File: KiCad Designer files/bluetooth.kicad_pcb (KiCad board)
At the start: 32 copper layers, 30.5 x 38.1 mm, 53 parts, among them U1 Multi-protocol Bluetooth Low 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, U1 O, U10 O, U11 O, U12 O, U13 O, U14 O, U15 O, U16 O, U17 O, U18 O, U19 O, U2 O, U20 O, U21 O, U22 O, U23 O, U24 O, U25 O, U26 O, U27 O, U28 O, U29 O, U3 O, U30 O, U31 O, U32 O, U33 O, U4 O, U5 O, U6 O, U7 O, U8 O, U9 O

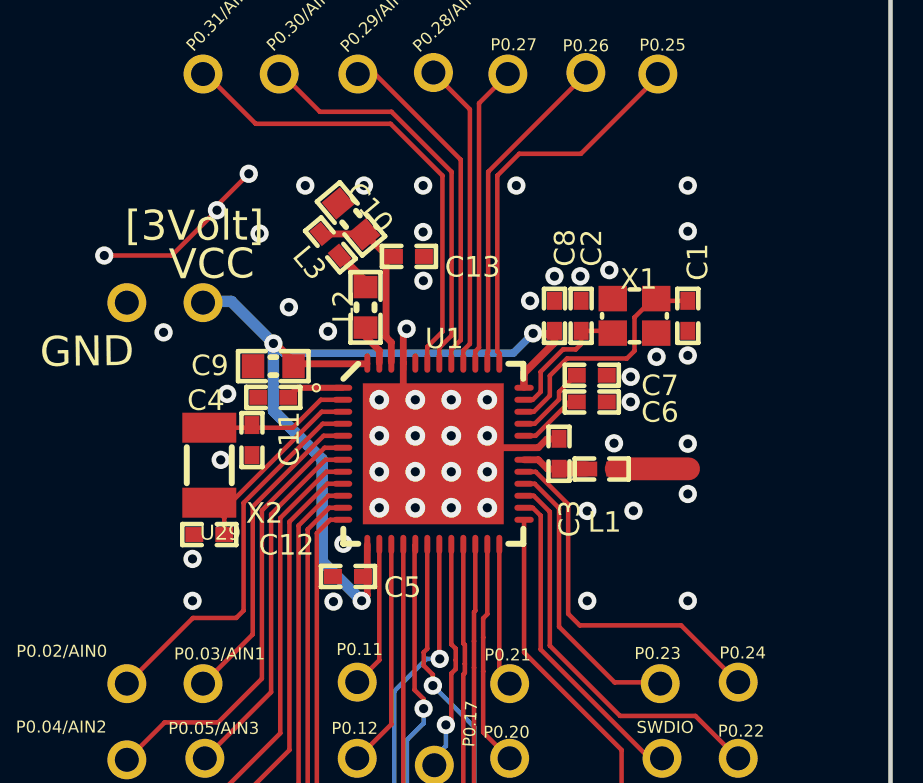
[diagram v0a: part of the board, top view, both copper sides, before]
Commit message: fixed KiCad pcb bugs and errors.
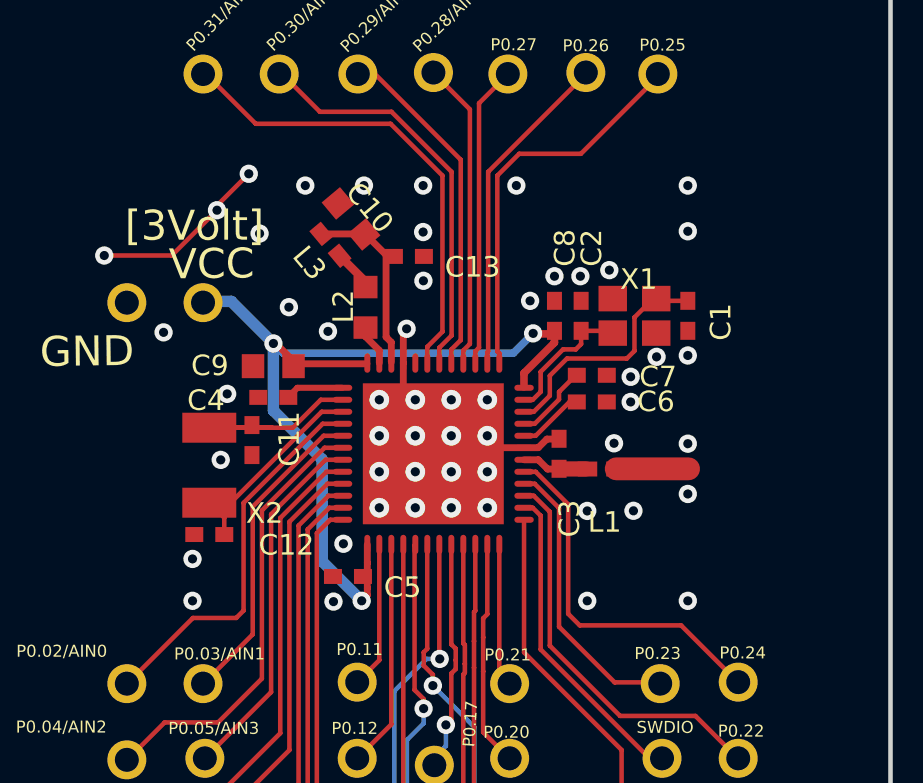
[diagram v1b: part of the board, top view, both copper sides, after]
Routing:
- net Net1: track 75.2 -> 0.00 mm
- net P0.00/XL1: track 4.83 -> 8.33 mm
- net VDD_NRF: track 30.3 -> 31.6 mm
- net P0.04/AIN2: vias 1 -> 0
- net GND: vias 52 -> 53
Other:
- board text removed: "U1"

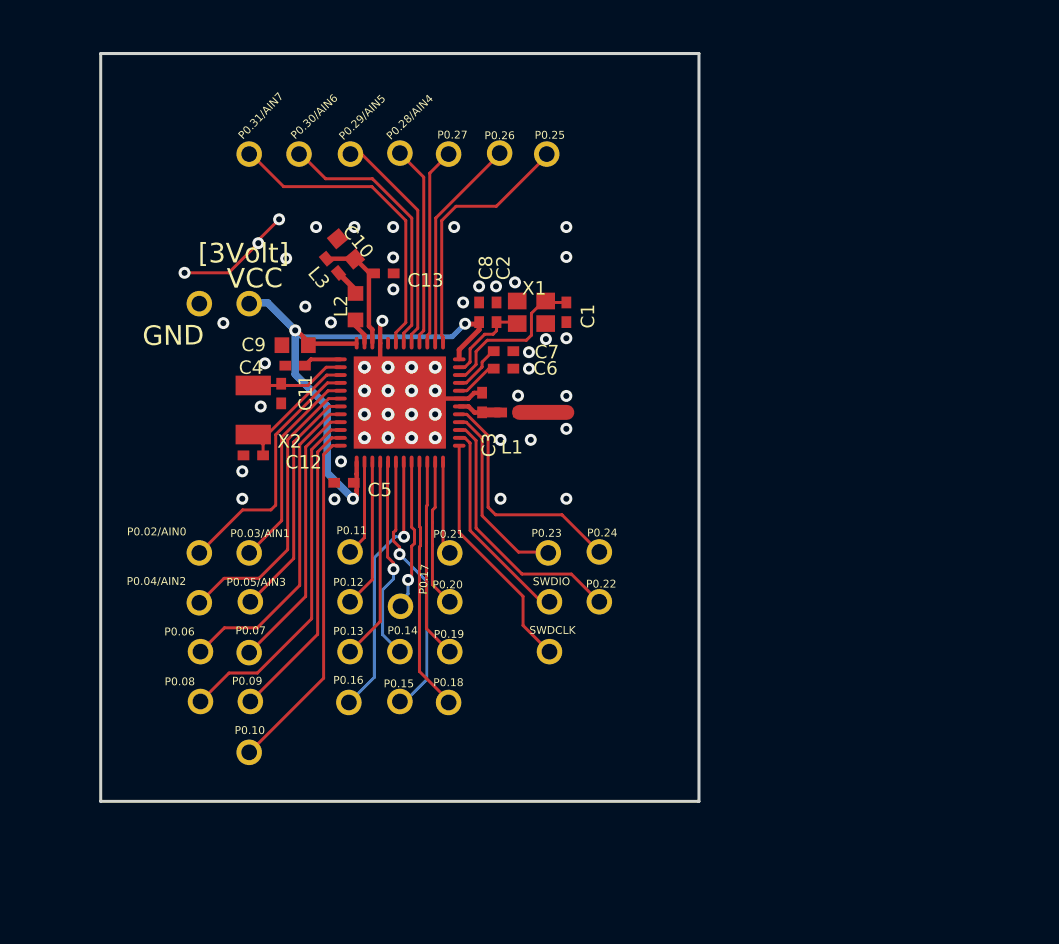
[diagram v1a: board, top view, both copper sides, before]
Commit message: added antenna to main pcb
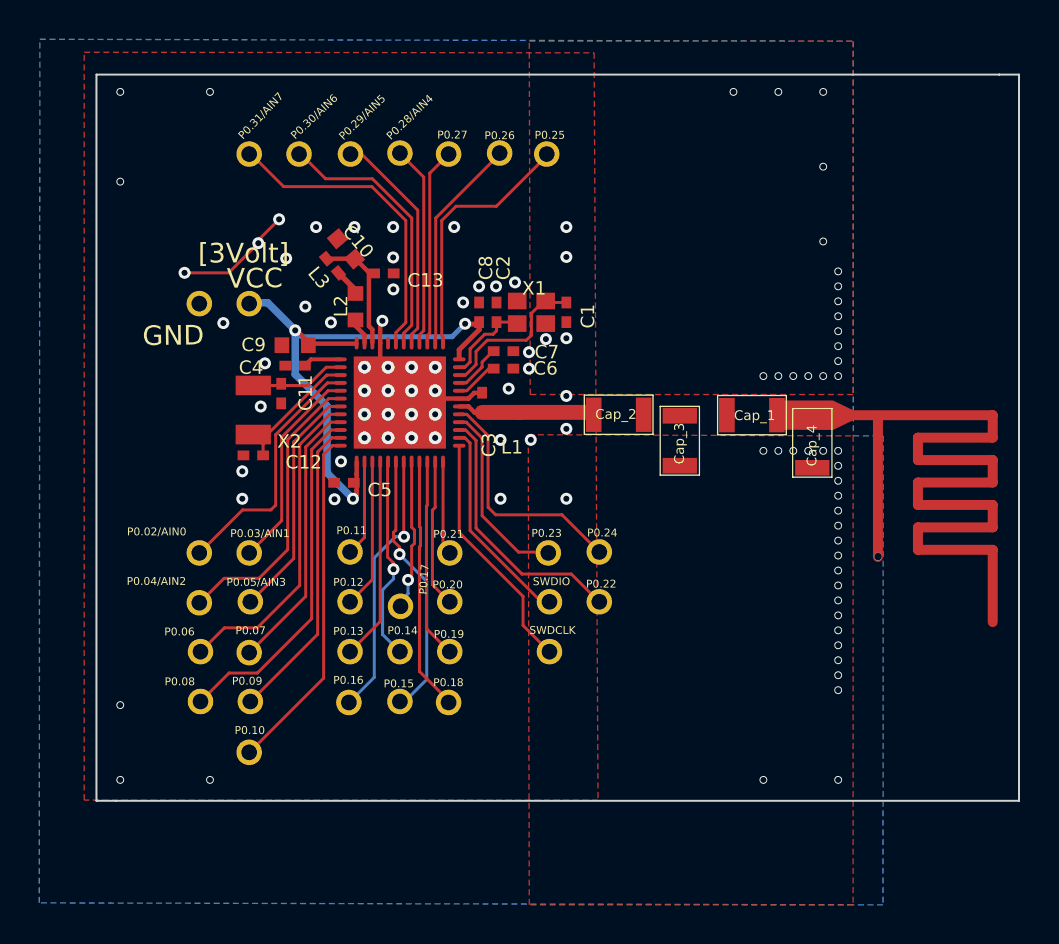
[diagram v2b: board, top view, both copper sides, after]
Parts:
- removed L1: , INDC1005X04L
- added Cap_1: 1206_cap_smd, Capacitors_smd:1206_cap_smd, F.Cu at (102.0, -84.8)
- added Cap_2: 1206_cap_smd, Capacitors_smd:1206_cap_smd, F.Cu at (95.3, -84.9)
- added Cap_3: 1206_cap_smd, Capacitors_smd:1206_cap_smd, F.Cu at (98.4, -83.5)
- added Cap_4: 1206_cap_smd, Capacitors_smd:1206_cap_smd, F.Cu at (105.1, -83.4)
- renumbered U22 to U102
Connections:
- C3 pad 2: NetC3_2 -> (no net)
- U1 pad 30: NetC3_2 -> (no net)
- U2 pad 1: Net-(U15-Pad1) -> Net-(U2-Pad1)
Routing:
- net GND: track 43.0 -> 90.8 mm, vias 53 -> 102
- net (no net): track 357.8 -> 362.4 mm
- net NetC3_2: track 2.20 -> 0.00 mm
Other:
- board size 30.5 x 38.1 mm -> 47 x 37 mm
- board text added: "60.579, 49.022"
